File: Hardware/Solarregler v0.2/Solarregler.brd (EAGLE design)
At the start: 99.3 x 80 mm, 89 parts, among them IC1-1 STM32F105RBT6, IC2-1 MCP2551-E/SN or SN65HVD230D, IC2-2 J-LINK-10PIN-HOLES, IC2-3 PRTR5V0U4D, IC5-1 MAX31865ATP+, IC5-2 MAX31865ATP+, IC6-1 MAX31865ATP+, Q1-1 8 MHz, Q1-2 32.768kHz, T3-1 PDTC124EU, U4 HUTSCHIENE_DEV

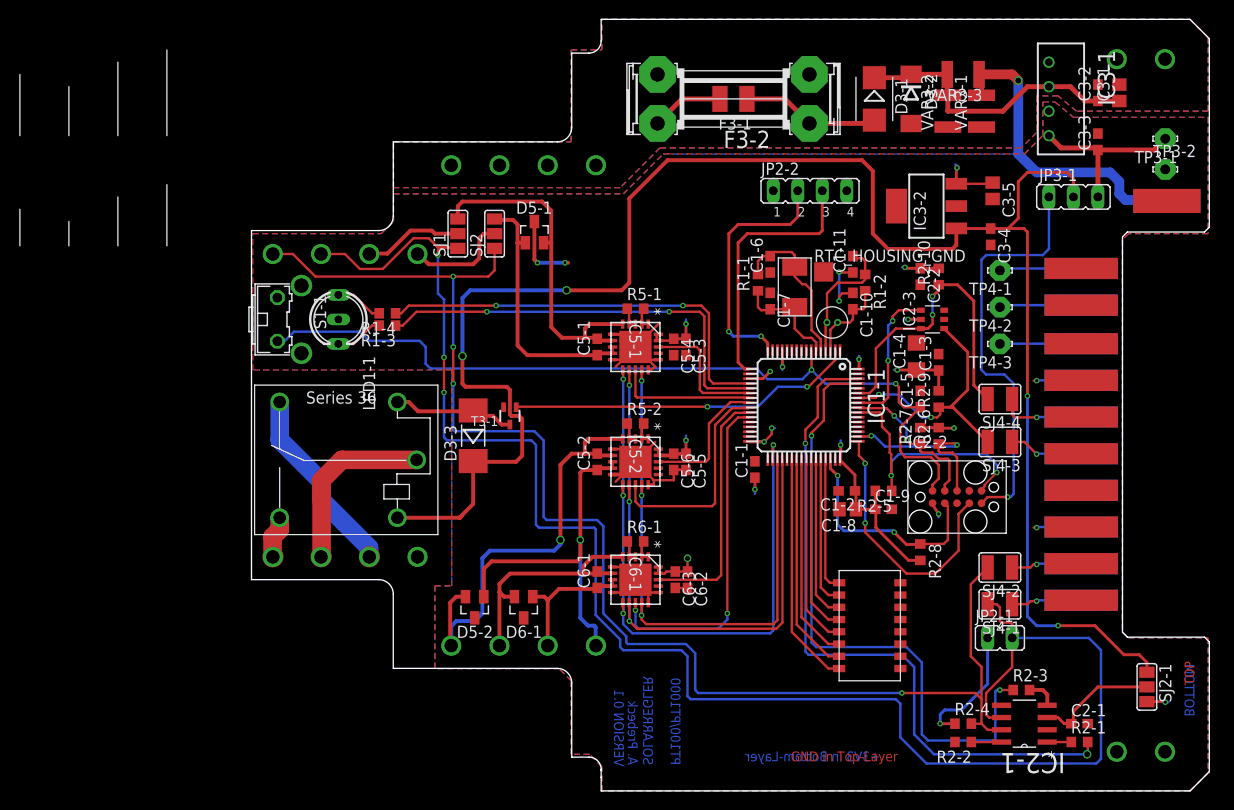
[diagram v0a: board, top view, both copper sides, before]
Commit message: Layout update nach Gespräch mit ME
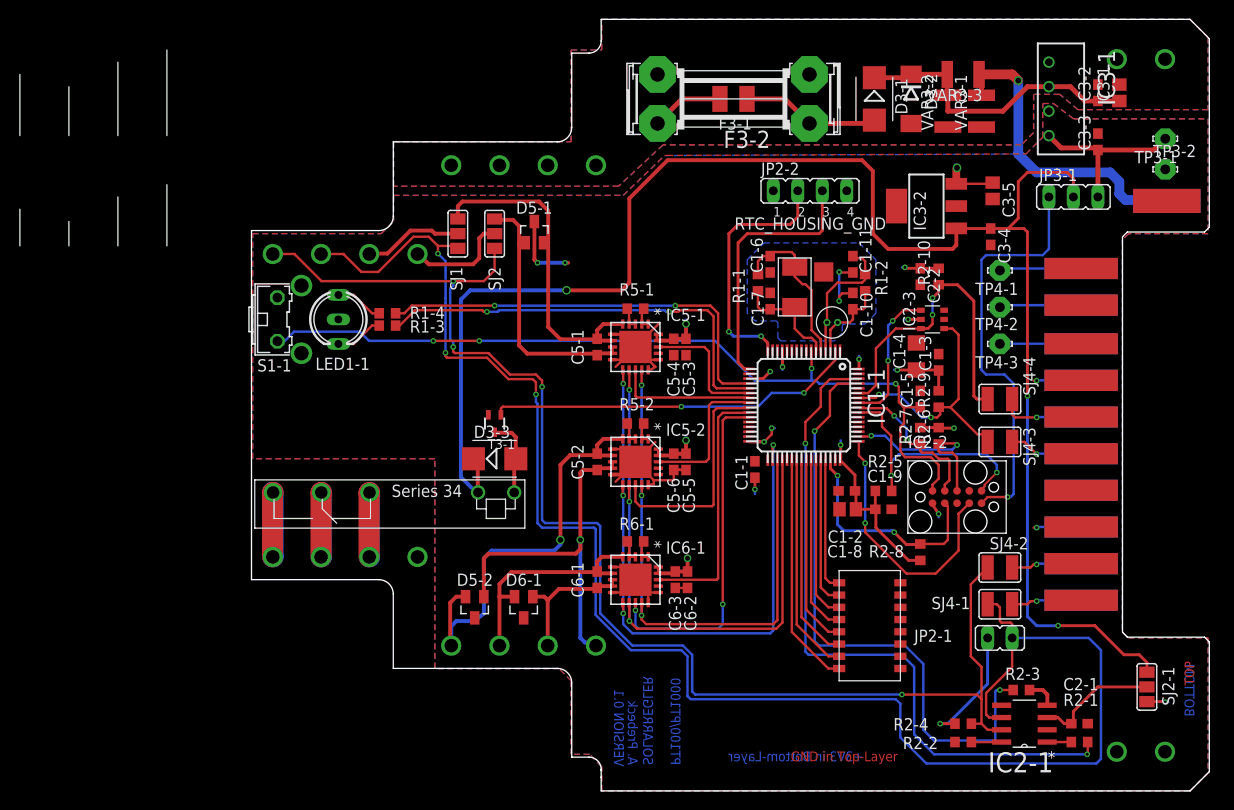
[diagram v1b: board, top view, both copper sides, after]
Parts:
- removed U$3: FINDER_36.11, 000_eigene_Bauteile:SERIES_36
- added U$2: FINDER_34.51, 000_eigene_Bauteile:SERIES_34
- D3-3: device diode:MELF-MLL41 -> diode:SMB
- moved D3-3 3.26 mm to (51.8, 33.8), turned to 0 degrees
- moved T3-1 1.77 mm to (51.8, 37.5)
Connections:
- net +5V: now also U$2.A1; no longer U$3.A1
- net N$10: now also U$2.A2; no longer U$3.A2
- net RELAIS_COM: now also U$2.11; no longer U$3.11
- net RELAIS_NC: now also U$2.12; no longer U$3.12
- net RELAIS_NO: now also U$2.14; no longer U$3.14
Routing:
- net +5V: track 188.7 -> 172.9 mm, vias 4 -> 3
- net RELAIS_NO: track 4.42 -> 13.4 mm
- net RELAIS_NC: track 19.9 -> 13.4 mm
- net RELAIS_COM: track 18.7 -> 13.4 mm
- net N$10: track 12.7 -> 8.21 mm
- net CANL: track 173.4 -> 170.1 mm
- net RELAIS_ON: track 36.1 -> 38.5 mm
- net RTD3+: track 25.7 -> 24.2 mm
- net RTD1+: track 36.7 -> 35.1 mm
- net RTD2+: track 46.0 -> 44.6 mm
- net NRST: track 88.1 -> 86.7 mm, vias 2 -> 4
- net CAN_RX: track 65.3 -> 63.9 mm
- net CANH: track 142.1 -> 140.9 mm
- net DRDY_2: track 14.1 -> 15.2 mm
- net CS_2: track 22.7 -> 23.6 mm
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- added copper zone on layer 16, net GND
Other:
- board text added: "CAN-ID 8-1"
- board text added: "CAN_TERM"
- board text added: "IC1"
- board text added: "IC2"
- board text added: "IC3"
- board text removed: "CAN-ID SWITCH 8-1"
- board text removed: "JP2-1"
- board text removed: "SJ2-1"
- board text removed: "SJ4-1"
- board text removed: "SJ4-2"
